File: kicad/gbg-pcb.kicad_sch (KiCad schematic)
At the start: 71 parts, among them J1 12 2.54mm pitch header pins, J100 0197054001, J101 0197054001, J102 0197054001, J103 0197054001, J104 wellye style, J105 wellye RX25 style, J11 Conn_01x10_Pin, J2 Conn_01x04, J3 joystick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

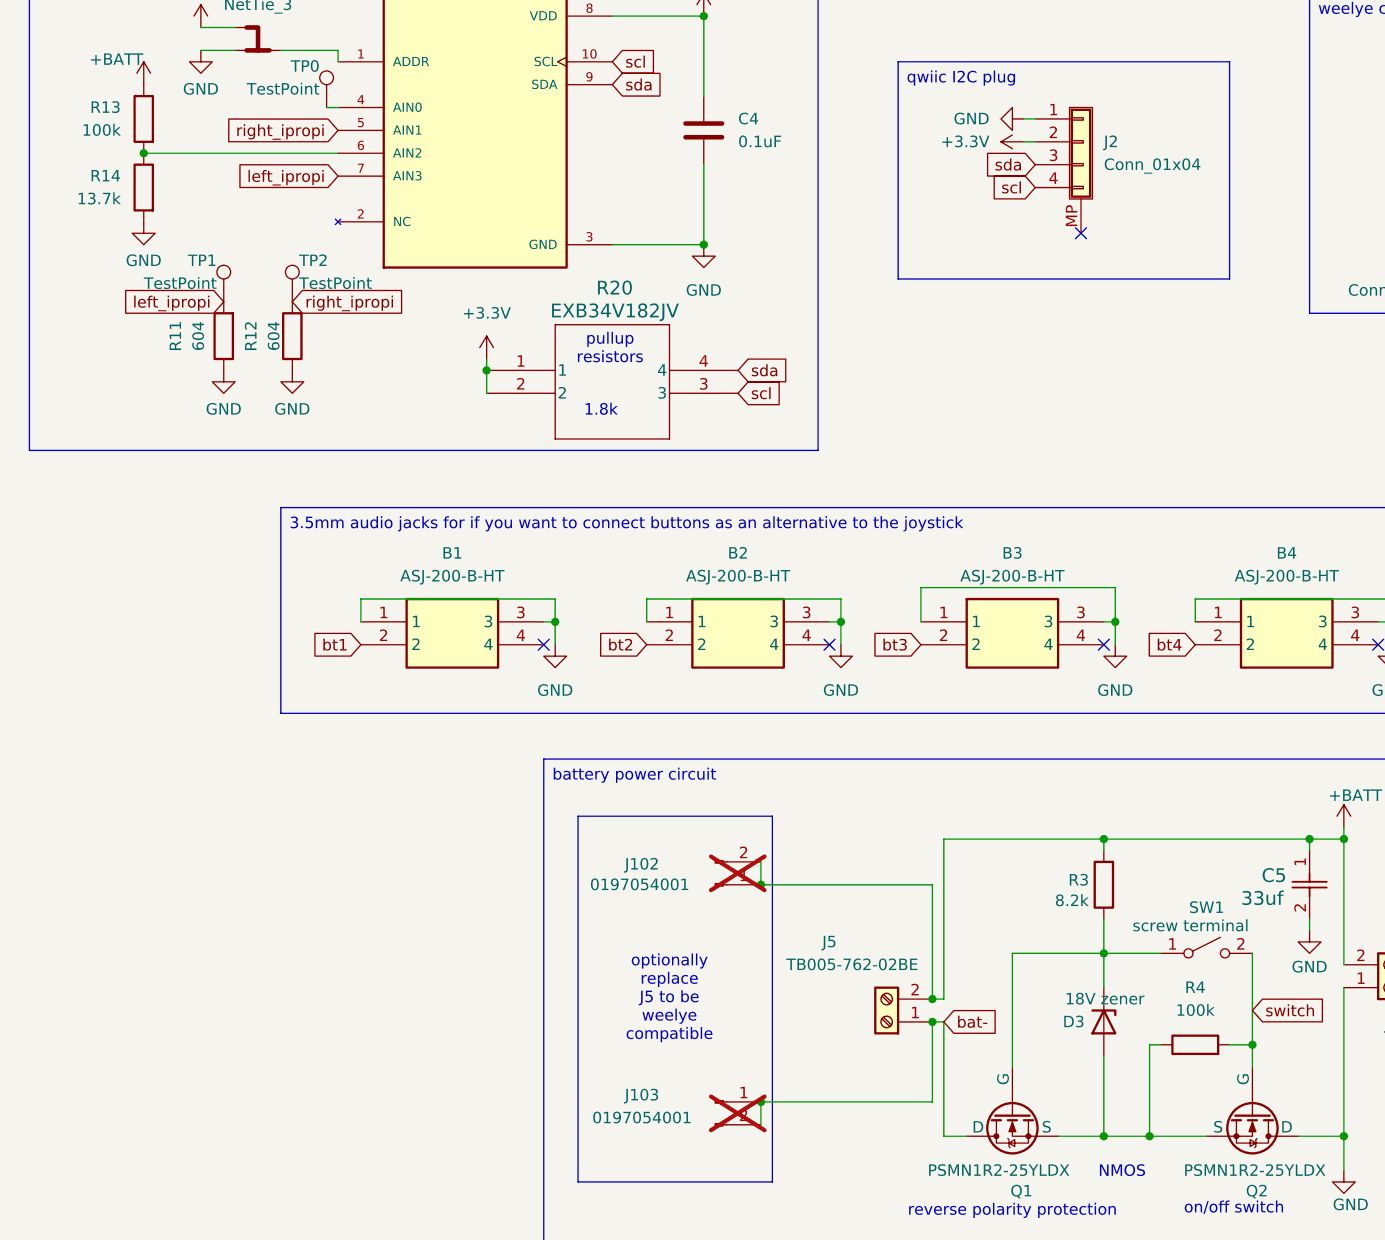
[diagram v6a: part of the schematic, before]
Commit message: change resistors
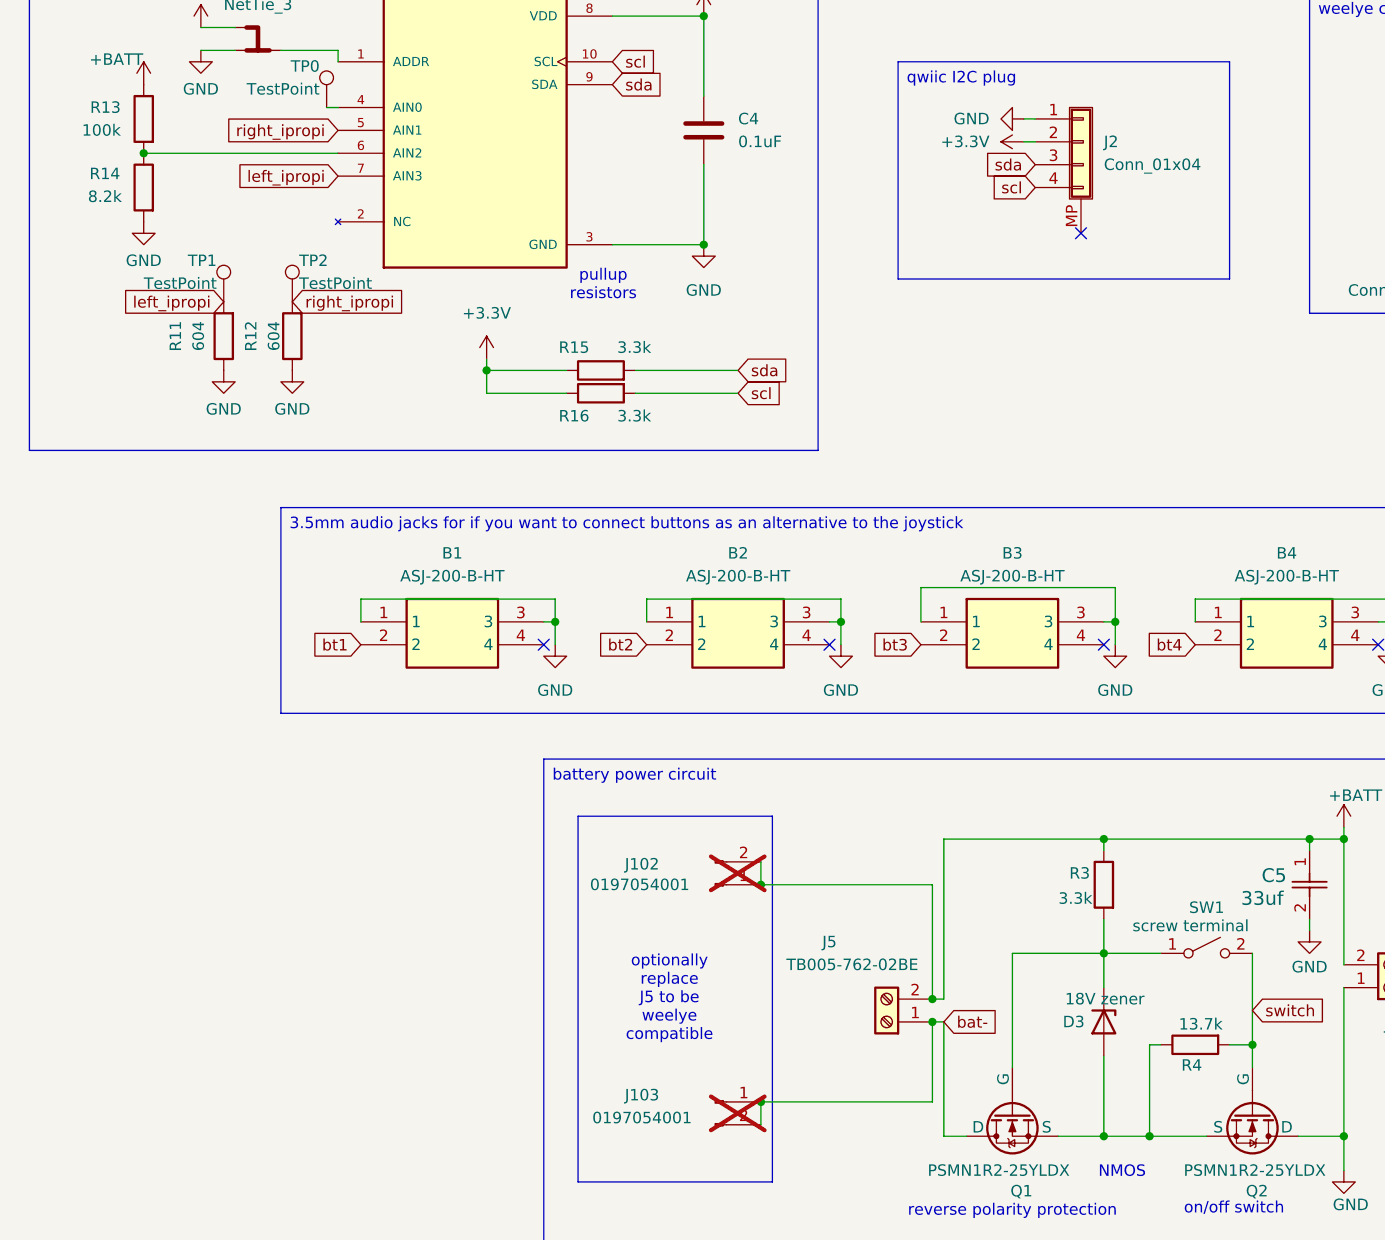
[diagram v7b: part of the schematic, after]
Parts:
- removed R20: EXB34V182JV, kicad libraries:C_ARRAY_EXB34V_PAN, symbol library:EXB34V182JV
- added R15, R16: 3.3k, Resistor_SMD:R_0805_2012Metric, symbol Device:R
- R14: value 13.7k -> 8.2k; Manufacturer_Part_Number CRCW080513K7FKEA -> CRCW08058K20JNEA; digikey_part_number 541-13.7KCCT-ND -> 541-8.2KACT-ND
- R3: value 8.2k -> 3.3k; Manufacturer_Part_Number CRCW08058K20JNEA -> CRCW08053K30FKEA; digikey_part_number 541-8.2KACT-ND -> 541-3.30KCCT-ND; price .04 -> .05
- R4: value 100k -> 13.7k; Manufacturer_Part_Number CRCW0805100KFKEA -> CRCW080513K7FKEA; digikey_part_number 541-100KCCT-ND -> 541-13.7KCCT-ND
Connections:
- net +3.3V: now also R15.1, R16.1
- net +BATT: now also R3.1; no longer R3.2
- net scl: now also R16.2
- net sda: now also R15.2
- net at D3.1 (K), Q1.4 (G), SW1.1 (A): now also R3.2; no longer R3.1
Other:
- note removed: "1.8k"

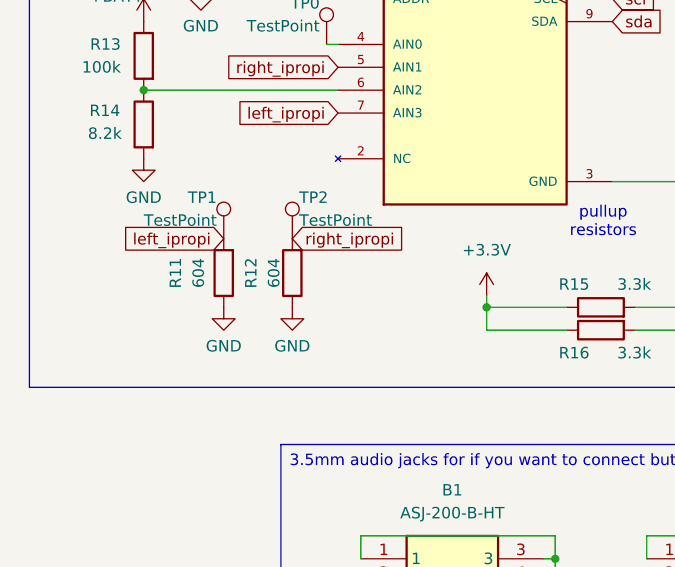
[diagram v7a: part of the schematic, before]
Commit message: adjust layout and heatsink pads
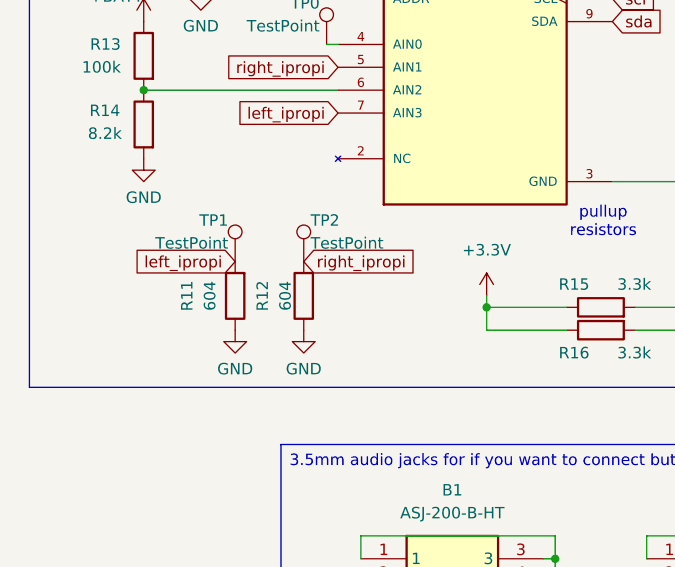
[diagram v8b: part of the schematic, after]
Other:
- moved on the sheet: R11, R12, TP1, TP2
